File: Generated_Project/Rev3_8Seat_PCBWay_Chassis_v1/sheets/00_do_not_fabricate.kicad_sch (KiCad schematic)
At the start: 0 parts

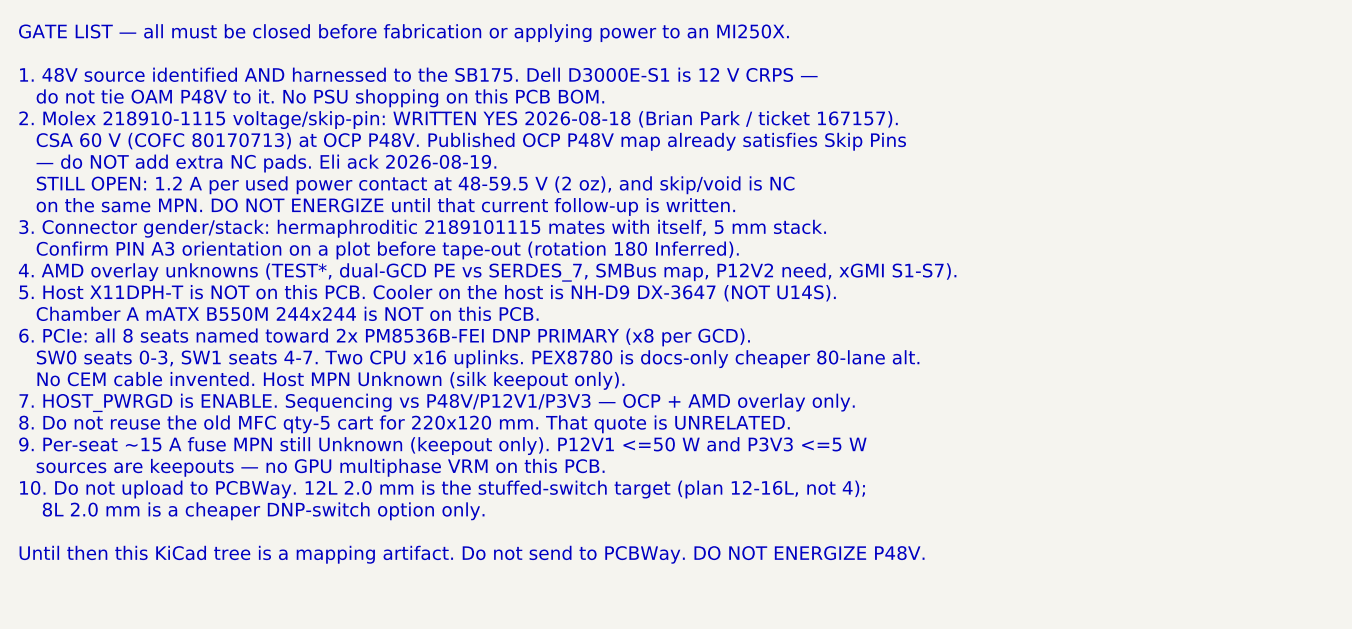
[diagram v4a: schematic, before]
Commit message: Add PCBWay-submittable POWER+MECH fab package for the Rev3 8-seat chassis.
Star-fed P48V (SB175 6325G1 + 2x 1382, per-seat 0476015.MR, local Conn0 pours),
THL 40-4812WI and OKI-78SR bucks, filled 12L 2.0 mm Gerbers/drill/IPC-356/PnP.
PM8536 stays DNP. Silk keeps DO NOT ENERGIZE P48V. Do not upload from this agent.

Co-authored-by: zivzancoeli-commits <zivzancoeli-commits@users.noreply.github.com>
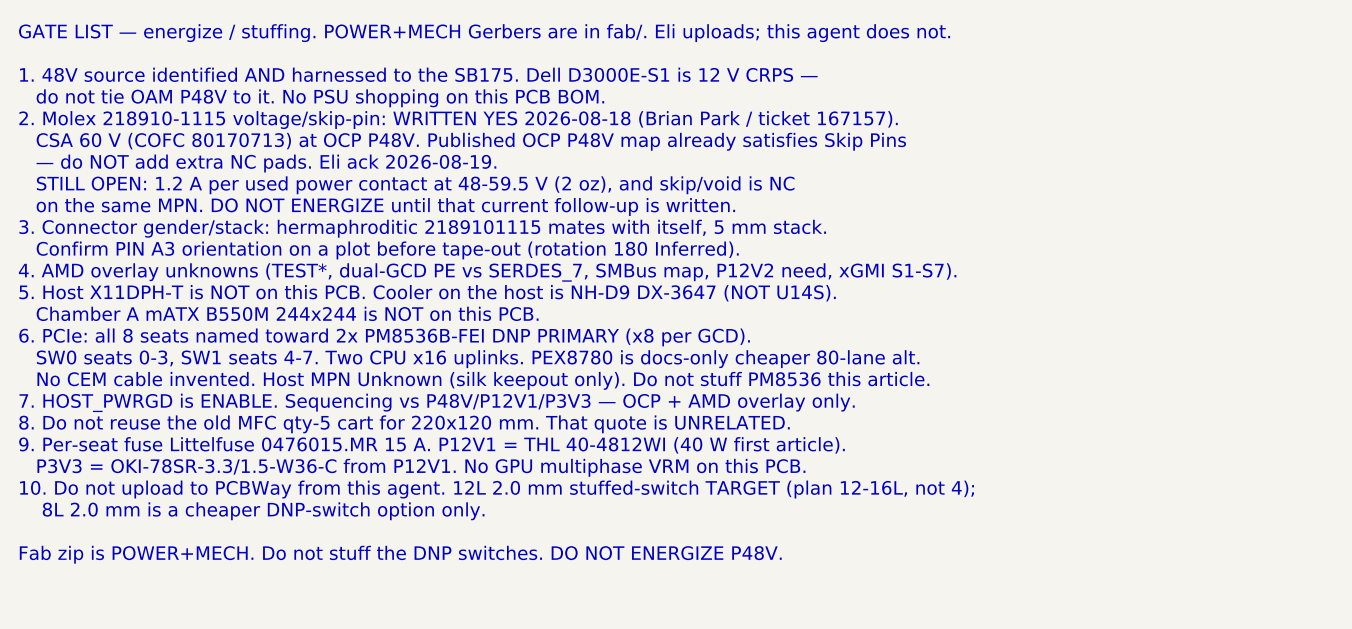
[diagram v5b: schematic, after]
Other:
- note added: "GATE LIST — energize / stuffing. POWER+MECH Gerbers are in fab/. Eli uploads; this agent does not. 1. 48V source identified AND harnessed to the SB175. Dell D3000E-S1 is 12 V CRPS — do not tie OAM P48V to it. No PSU shopping on this PCB BOM. 2. Molex 218910-1115 voltage/skip-pin: WRITTEN YES 2026-08-18 (Brian Park / ticket 167157). CSA 60 V (COFC 80170713) at OCP P48V. Published OCP P48V map alre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"
- note removed: "GATE LIST — all must be closed before fabrication or applying power to an MI250X. 1. 48V source identified AND harnessed to the SB175. Dell D3000E-S1 is 12 V CRPS — do not tie OAM P48V to it. No PSU shopping on this PCB BOM. 2. Molex 218910-1115 voltage/skip-pin: WRITTEN YES 2026-08-18 (Brian Park / ticket 167157). CSA 60 V (COFC 80170713) at OCP P48V. Published OCP P48V map already satisfies Ski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"
- title: DO NOT FABRICATE -> ENERGIZE / STUFFING GATES (fab zip in fab/)
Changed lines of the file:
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@@
 	(paper "A3")
 	(title_block
-		(title "DO NOT FABRICATE")
+		(title "ENERGIZE / STUFFING GATES (fab zip in fab/)")
 		(date "2026-08-22")
 		(rev "Rev3_8Seat_PCBWay_v1")
-        (comment 1 "DO NOT FABRICATE. DO NOT ENERGIZE P48V. Molex 60V written 2026-08-18; 1.2A/contact OPEN.")
+        (comment 1 "DO NOT ENERGIZE P48V. Molex 60V written 2026-08-18; 1.2A/contact OPEN. Skip-pin NC.")
         (comment 2 "Documentation sheet — no invented nets")
         (comment 3 "Pin names: OAM Pin map rev 1.0.xlsx — OCP generic, NOT AMD overlay")
         (comment 4 "r2.0 UNUSABLE. P3V3=Conn0 C1/C2. 12L 2.0mm stuffed-switch TARGET. 2x PM8536 DNP. Star-fed P48V.")
 	)
-	(text "GATE LIST — all must be closed before fabrication or applying power to an MI250X.\n\n1. 48V source identified AND harnessed to the SB175. Dell D3000E-S1 is 12 V CRPS —\n   do not tie OAM P48V to it. No PSU shopping on this PCB BOM.\n2. Molex 218910-1115 voltage/skip-pin: WRITTEN YES 2026-08-18 (Brian Park / ticket 167157).\n   CSA 60 V (COFC 80170713) at OCP P48V. Published OCP P48V map already satisfies Skip Pins\n   — do NOT add extra NC pads. Eli ack 2026-08-19.\n   STILL OPEN: 1.2 A per used power contact at 48-59.5 V (2 oz), and skip/void is NC\n   on the same MPN. DO NOT ENERGIZE until that current follow-up is written.\n3. Connector gender/stack: hermaphroditic 2189101115 mates with itself, 5 mm stack.\n   Confirm PIN A3 orientation on a plot before tape-out (rotation 180 Inferred).\n4. AMD overlay unknowns (TEST*, dual-GCD PE vs SERDES_7, SMBus map, P12V2 need, xGMI S1-S7).\n5. Host X11DPH-T is NOT on this PCB. Cooler on the host is NH-D9 DX-3647 (NOT U14S).\n   Chamber A mATX B550M 244x244 is NOT on this PCB.\n6. PCIe: all 8 seats named toward 2x PM8536B-FEI DNP PRIMARY (x8 per GCD).\n   SW0 seats 0-3, SW1 seats 4-7. Two CPU x16 uplinks. PEX8780 is docs-only cheaper 80-lane alt.\n   No CEM cable invented. Host MPN Unknown (silk keepout only).\n7. HOST_PWRGD is ENABLE. Sequencing vs P48V/P12V1/P3V3 — OCP + AMD overlay only.\n8. Do not reuse the old MFC qty-5 cart for 220x120 mm. That quote is UNRELATED.\n9. Per-seat ~15 A fuse MPN still Unknown (keepout only). P12V1 <=50 W and P3V3 <=5 W\n   sources are keepouts — no GPU multiphase VRM on this PCB.\n10. Do not upload to PCBWay. 12L 2.0 mm is the stuffed-switch target (plan 12-16L, not 4);\n    8L 2.0 mm is a cheaper DNP-switch option only.\n\nUntil then this KiCad tree is a mapping artifact. Do not send to PCBWay. DO NOT ENERGIZE P48V.\n"
+	(text "GATE LIST — energize / stuffing. POWER+MECH Gerbers are in fab/. Eli uploads; this agent does not.\n\n1. 48V source identified AND harnessed to the SB175. Dell D3000E-S1 is 12 V CRPS —\n   do not tie OAM P48V to it. No PSU shopping on this PCB BOM.\n2. Molex 218910-1115 voltage/skip-pin: WRITTEN YES 2026-08-18 (Brian Park / ticket 167157).\n   CSA 60 V (COFC 80170713) at OCP P48V. Published OCP P48V map already satisfies Skip Pins\n   — do NOT add extra NC pads. Eli ack 2026-08-19.\n   STILL OPEN: 1.2 A per used power contact at 48-59.5 V (2 oz), and skip/void is NC\n   on the same MPN. DO NOT ENERGIZE until that current follow-up is written.\n3. Connector gender/stack: hermaphroditic 2189101115 mates with itself, 5 mm stack.\n   Confirm PIN A3 orientation on a plot before tape-out (rotation 180 Inferred).\n4. AMD overlay unknowns (TEST*, dual-GCD PE vs SERDES_7, SMBus map, P12V2 need, xGMI S1-S7).\n5. Host X11DPH-T is NOT on this PCB. Cooler on the host is NH-D9 DX-3647 (NOT U14S).\n   Chamber A mATX B550M 244x244 is NOT on this PCB.\n6. PCIe: all 8 seats named toward 2x PM8536B-FEI DNP PRIMARY (x8 per GCD).\n   SW0 seats 0-3, SW1 seats 4-7. Two CPU x16 uplinks. PEX8780 is docs-only cheaper 80-lane alt.\n   No CEM cable invented. Host MPN Unknown (silk keepout only). Do not stuff PM8536 this article.\n7. HOST_PWRGD is ENABLE. Sequencing vs P48V/P12V1/P3V3 — OCP + AMD overlay only.\n8. Do not reuse the old MFC qty-5 cart for 220x120 mm. That quote is UNRELATED.\n9. Per-seat fuse Littelfuse 0476015.MR 15 A. P12V1 = THL 40-4812WI (40 W first article).\n   P3V3 = OKI-78SR-3.3/1.5-W36-C from P12V1. No GPU multiphase VRM on this PCB.\n10. Do not upload to PCBWay from this agent. 12L 2.0 mm stuffed-switch TARGET (plan 12-16L, not 4);\n    8L 2.0 mm is a cheaper DNP-switch option only.\n\nFab zip is POWER+MECH. Do not stuff the DNP switches. DO NOT ENERGIZE P48V.\n"
 		(exclude_from_sim no)
 		(at 20.32 20.32 0)

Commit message: Make the Rev3 8-seat chassis full-width capable with four PM8536 DNP courtyards.
Same 492x372 POWER+MECH PCB; architecture is now 16 named x16 PE buses
(PE_Sn_GCD0_x16 + PE_Sn_GCD1_x16) and SW0-SW3 keepouts. Two 96-lane
switches are enough for 8x x8/GCD, not 8x x16/GCD. Host stays X11DPH-T
(~80 lanes) and cannot light 256 downstream. Do not energize P48V.

Co-authored-by: zivzancoeli-commits <zivzancoeli-commits@users.noreply.github.com>
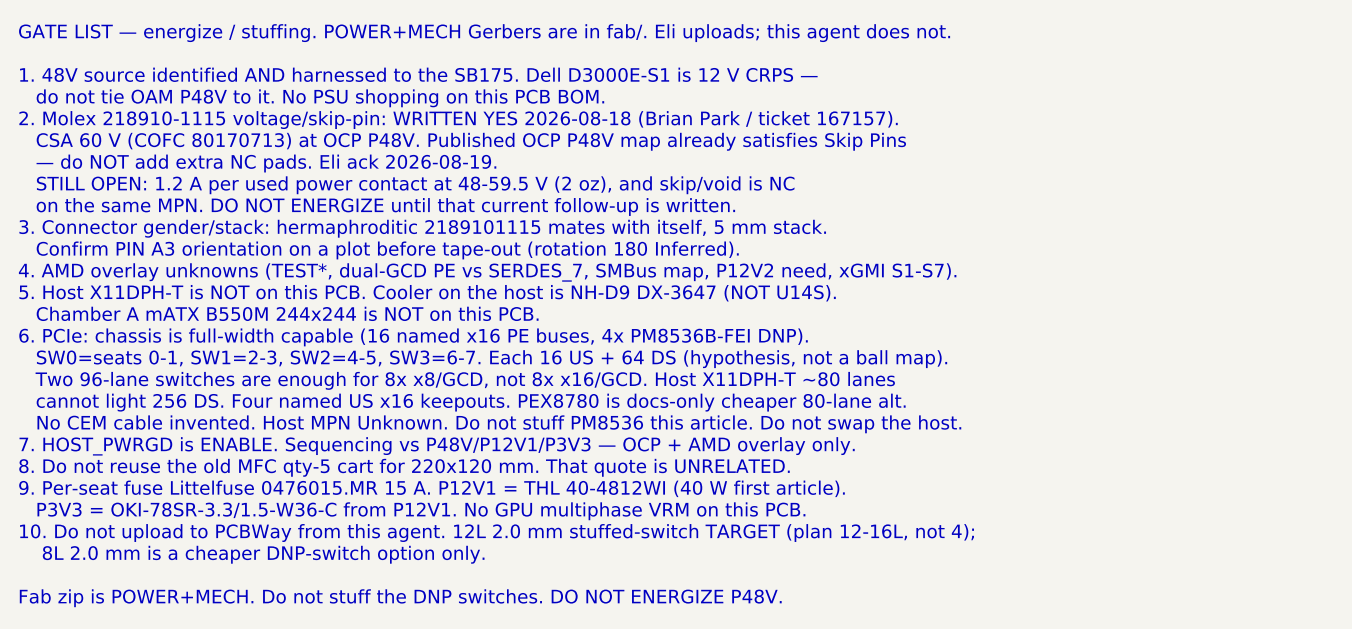
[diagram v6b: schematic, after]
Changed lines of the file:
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@@
         (comment 2 "Documentation sheet — no invented nets")
         (comment 3 "Pin names: OAM Pin map rev 1.0.xlsx — OCP generic, NOT AMD overlay")
-        (comment 4 "r2.0 UNUSABLE. P3V3=Conn0 C1/C2. 12L 2.0mm stuffed-switch TARGET. 2x PM8536 DNP. Star-fed P48V.")
+        (comment 4 "r2.0 UNUSABLE. P3V3=Conn0 C1/C2. 12L 2.0mm stuffed-switch TARGET. 4x PM8536 DNP. Star-fed P48V.")
 	)
-	(text "GATE LIST — energize / stuffing. POWER+MECH Gerbers are in fab/. Eli uploads; this agent does not.\n\n1. 48V source identified AND harnessed to the SB175. Dell D3000E-S1 is 12 V CRPS —\n   do not tie OAM P48V to it. No PSU shopping on this PCB BOM.\n2. Molex 218910-1115 voltage/skip-pin: WRITTEN YES 2026-08-18 (Brian Park / ticket 167157).\n   CSA 60 V (COFC 80170713) at OCP P48V. Published OCP P48V map already satisfies Skip Pins\n   — do NOT add extra NC pads. Eli ack 2026-08-19.\n   STILL OPEN: 1.2 A per used power contact at 48-59.5 V (2 oz), and skip/void is NC\n   on the same MPN. DO NOT ENERGIZE until that current follow-up is written.\n3. Connector gender/stack: hermaphroditic 2189101115 mates with itself, 5 mm stack.\n   Confirm PIN A3 orientation on a plot before tape-out (rotation 180 Inferred).\n4. AMD overlay unknowns (TEST*, dual-GCD PE vs SERDES_7, SMBus map, P12V2 need, xGMI S1-S7).\n5. Host X11DPH-T is NOT on this PCB. Cooler on the host is NH-D9 DX-3647 (NOT U14S).\n   Chamber A mATX B550M 244x244 is NOT on this PCB.\n6. PCIe: all 8 seats named toward 2x PM8536B-FEI DNP PRIMARY (x8 per GCD).\n   SW0 seats 0-3, SW1 seats 4-7. Two CPU x16 uplinks. PEX8780 is docs-only cheaper 80-lane alt.\n   No CEM cable invented. Host MPN Unknown (silk keepout only). Do not stuff PM8536 this article.\n7. HOST_PWRGD is ENABLE. Sequencing vs P48V/P12V1/P3V3 — OCP + AMD overlay only.\n8. Do not reuse the old MFC qty-5 cart for 220x120 mm. That quote is UNRELATED.\n9. Per-seat fuse Littelfuse 0476015.MR 15 A. P12V1 = THL 40-4812WI (40 W first article).\n   P3V3 = OKI-78SR-3.3/1.5-W36-C from P12V1. No GPU multiphase VRM on this PCB.\n10. Do not upload to PCBWay from this agent. 12L 2.0 mm stuffed-switch TARGET (plan 12-16L, not 4);\n    8L 2.0 mm is a cheaper DNP-switch option only.\n\nFab zip is POWER+MECH. Do not stuff the DNP switches. DO NOT ENERGIZE P48V.\n"
+	(text "GATE LIST — energize / stuffing. POWER+MECH Gerbers are in fab/. Eli uploads; this agent does not.\n\n1. 48V source identified AND harnessed to the SB175. Dell D3000E-S1 is 12 V CRPS —\n   do not tie OAM P48V to it. No PSU shopping on this PCB BOM.\n2. Molex 218910-1115 voltage/skip-pin: WRITTEN YES 2026-08-18 (Brian Park / ticket 167157).\n   CSA 60 V (COFC 80170713) at OCP P48V. Published OCP P48V map already satisfies Skip Pins\n   — do NOT add extra NC pads. Eli ack 2026-08-19.\n   STILL OPEN: 1.2 A per used power contact at 48-59.5 V (2 oz), and skip/void is NC\n   on the same MPN. DO NOT ENERGIZE until that current follow-up is written.\n3. Connector gender/stack: hermaphroditic 2189101115 mates with itself, 5 mm stack.\n   Confirm PIN A3 orientation on a plot before tape-out (rotation 180 Inferred).\n4. AMD overlay unknowns (TEST*, dual-GCD PE vs SERDES_7, SMBus map, P12V2 need, xGMI S1-S7).\n5. Host X11DPH-T is NOT on this PCB. Cooler on the host is NH-D9 DX-3647 (NOT U14S).\n   Chamber A mATX B550M 244x244 is NOT on this PCB.\n6. PCIe: chassis is full-width capable (16 named x16 PE buses, 4x PM8536B-FEI DNP).\n   SW0=seats 0-1, SW1=2-3, SW2=4-5, SW3=6-7. Each 16 US + 64 DS (hypothesis, not a ball map).\n   Two 96-lane switches are enough for 8x x8/GCD, not 8x x16/GCD. Host X11DPH-T ~80 lanes\n   cannot light 256 DS. Four named US x16 keepouts. PEX8780 is docs-only cheaper 80-lane alt.\n   No CEM cable invented. Host MPN Unknown. Do not stuff PM8536 this article. Do not swap the host.\n7. HOST_PWRGD is ENABLE. Sequencing vs P48V/P12V1/P3V3 — OCP + AMD overlay only.\n8. Do not reuse the old MFC qty-5 cart for 220x120 mm. That quote is UNRELATED.\n9. Per-seat fuse Littelfuse 0476015.MR 15 A. P12V1 = THL 40-4812WI (40 W first article).\n   P3V3 = OKI-78SR-3.3/1.5-W36-C from P12V1. No GPU multiphase VRM on this PCB.\n10. Do not upload to PCBWay from this agent. 12L 2.0 mm stuffed-switch TARGET (plan 12-16L, not 4);\n    8L 2.0 mm is a cheaper DNP-switch option only.\n\nFab zip is POWER+MECH. Do not stuff the DNP switches. DO NOT ENERGIZE P48V.\n"
 		(exclude_from_sim no)
 		(at 20.32 20.32 0)

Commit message: Retarget Rev3 first article to seats 0-1 GCD0 x16 (2-module path).
Same 8-seat PCB. Without overlay, 2x MI250X means two modules can sit
and at most GCD0 on each can be named toward the host keepout (2 GCDs),
not 2x full-width (4 GCDs). Conn0 OCP PCIE_* is the only legal host PE.
No CEM/MCIO MPN. Do not energize P48V.

Co-authored-by: zivzancoeli-commits <zivzancoeli-commits@users.noreply.github.com>
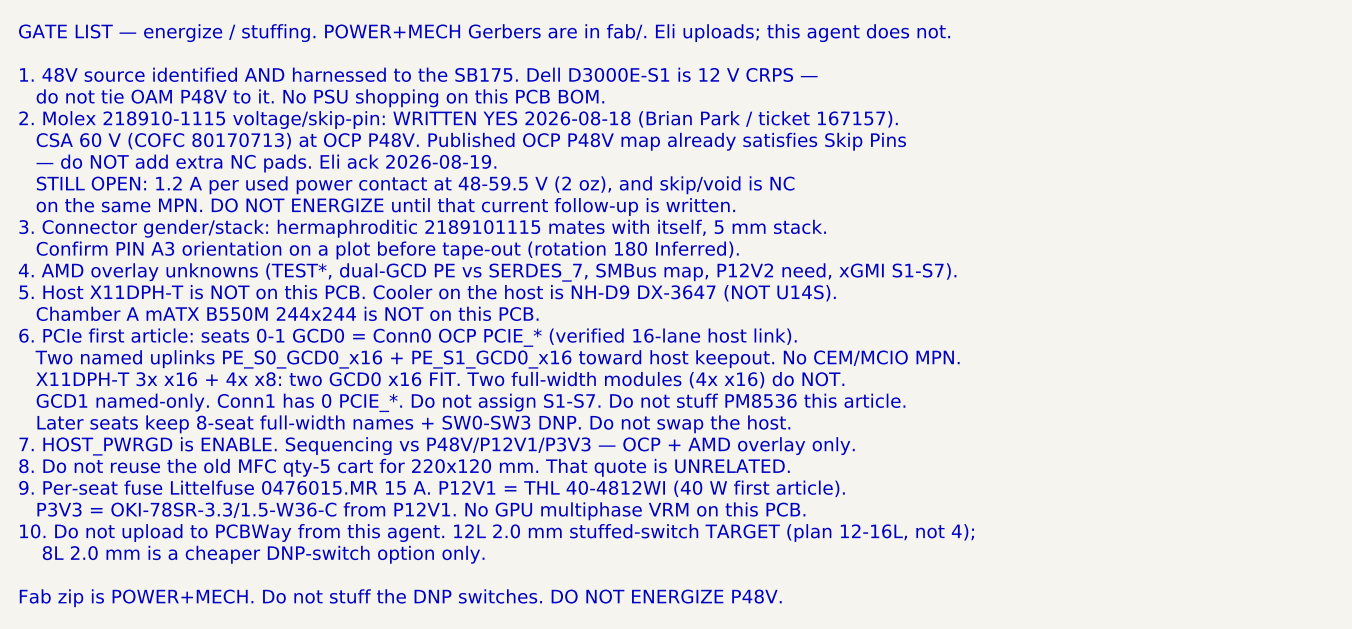
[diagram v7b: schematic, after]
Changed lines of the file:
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@@
         (comment 4 "r2.0 UNUSABLE. P3V3=Conn0 C1/C2. 12L 2.0mm stuffed-switch TARGET. 4x PM8536 DNP. Star-fed P48V.")
 	)
-	(text "GATE LIST — energize / stuffing. POWER+MECH Gerbers are in fab/. Eli uploads; this agent does not.\n\n1. 48V source identified AND harnessed to the SB175. Dell D3000E-S1 is 12 V CRPS —\n   do not tie OAM P48V to it. No PSU shopping on this PCB BOM.\n2. Molex 218910-1115 voltage/skip-pin: WRITTEN YES 2026-08-18 (Brian Park / ticket 167157).\n   CSA 60 V (COFC 80170713) at OCP P48V. Published OCP P48V map already satisfies Skip Pins\n   — do NOT add extra NC pads. Eli ack 2026-08-19.\n   STILL OPEN: 1.2 A per used power contact at 48-59.5 V (2 oz), and skip/void is NC\n   on the same MPN. DO NOT ENERGIZE until that current follow-up is written.\n3. Connector gender/stack: hermaphroditic 2189101115 mates with itself, 5 mm stack.\n   Confirm PIN A3 orientation on a plot before tape-out (rotation 180 Inferred).\n4. AMD overlay unknowns (TEST*, dual-GCD PE vs SERDES_7, SMBus map, P12V2 need, xGMI S1-S7).\n5. Host X11DPH-T is NOT on this PCB. Cooler on the host is NH-D9 DX-3647 (NOT U14S).\n   Chamber A mATX B550M 244x244 is NOT on this PCB.\n6. PCIe: chassis is full-width capable (16 named x16 PE buses, 4x PM8536B-FEI DNP).\n   SW0=seats 0-1, SW1=2-3, SW2=4-5, SW3=6-7. Each 16 US + 64 DS (hypothesis, not a ball map).\n   Two 96-lane switches are enough for 8x x8/GCD, not 8x x16/GCD. Host X11DPH-T ~80 lanes\n   cannot light 256 DS. Four named US x16 keepouts. PEX8780 is docs-only cheaper 80-lane alt.\n   No CEM cable invented. Host MPN Unknown. Do not stuff PM8536 this article. Do not swap the host.\n7. HOST_PWRGD is ENABLE. Sequencing vs P48V/P12V1/P3V3 — OCP + AMD overlay only.\n8. Do not reuse the old MFC qty-5 cart for 220x120 mm. That quote is UNRELATED.\n9. Per-seat fuse Littelfuse 0476015.MR 15 A. P12V1 = THL 40-4812WI (40 W first article).\n   P3V3 = OKI-78SR-3.3/1.5-W36-C from P12V1. No GPU multiphase VRM on this PCB.\n10. Do not upload to PCBWay from this agent. 12L 2.0 mm stuffed-switch TARGET (plan 12-16L, not 4);\n    8L 2.0 mm is a cheaper DNP-switch option only.\n\nFab zip is POWER+MECH. Do not stuff the DNP switches. DO NOT ENERGIZE P48V.\n"
+	(text "GATE LIST — energize / stuffing. POWER+MECH Gerbers are in fab/. Eli uploads; this agent does not.\n\n1. 48V source identified AND harnessed to the SB175. Dell D3000E-S1 is 12 V CRPS —\n   do not tie OAM P48V to it. No PSU shopping on this PCB BOM.\n2. Molex 218910-1115 voltage/skip-pin: WRITTEN YES 2026-08-18 (Brian Park / ticket 167157).\n   CSA 60 V (COFC 80170713) at OCP P48V. Published OCP P48V map already satisfies Skip Pins\n   — do NOT add extra NC pads. Eli ack 2026-08-19.\n   STILL OPEN: 1.2 A per used power contact at 48-59.5 V (2 oz), and skip/void is NC\n   on the same MPN. DO NOT ENERGIZE until that current follow-up is written.\n3. Connector gender/stack: hermaphroditic 2189101115 mates with itself, 5 mm stack.\n   Confirm PIN A3 orientation on a plot before tape-out (rotation 180 Inferred).\n4. AMD overlay unknowns (TEST*, dual-GCD PE vs SERDES_7, SMBus map, P12V2 need, xGMI S1-S7).\n5. Host X11DPH-T is NOT on this PCB. Cooler on the host is NH-D9 DX-3647 (NOT U14S).\n   Chamber A mATX B550M 244x244 is NOT on this PCB.\n6. PCIe first article: seats 0-1 GCD0 = Conn0 OCP PCIE_* (verified 16-lane host link).\n   Two named uplinks PE_S0_GCD0_x16 + PE_S1_GCD0_x16 toward host keepout. No CEM/MCIO MPN.\n   X11DPH-T 3x x16 + 4x x8: two GCD0 x16 FIT. Two full-width modules (4x x16) do NOT.\n   GCD1 named-only. Conn1 has 0 PCIE_*. Do not assign S1-S7. Do not stuff PM8536 this article.\n   Later seats keep 8-seat full-width names + SW0-SW3 DNP. Do not swap the host.\n7. HOST_PWRGD is ENABLE. Sequencing vs P48V/P12V1/P3V3 — OCP + AMD overlay only.\n8. Do not reuse the old MFC qty-5 cart for 220x120 mm. That quote is UNRELATED.\n9. Per-seat fuse Littelfuse 0476015.MR 15 A. P12V1 = THL 40-4812WI (40 W first article).\n   P3V3 = OKI-78SR-3.3/1.5-W36-C from P12V1. No GPU multiphase VRM on this PCB.\n10. Do not upload to PCBWay from this agent. 12L 2.0 mm stuffed-switch TARGET (plan 12-16L, not 4);\n    8L 2.0 mm is a cheaper DNP-switch option only.\n\nFab zip is POWER+MECH. Do not stuff the DNP switches. DO NOT ENERGIZE P48V.\n"
 		(exclude_from_sim no)
 		(at 20.32 20.32 0)
